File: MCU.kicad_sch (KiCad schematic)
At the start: 1 part, among them U20 STM32H562RGTx

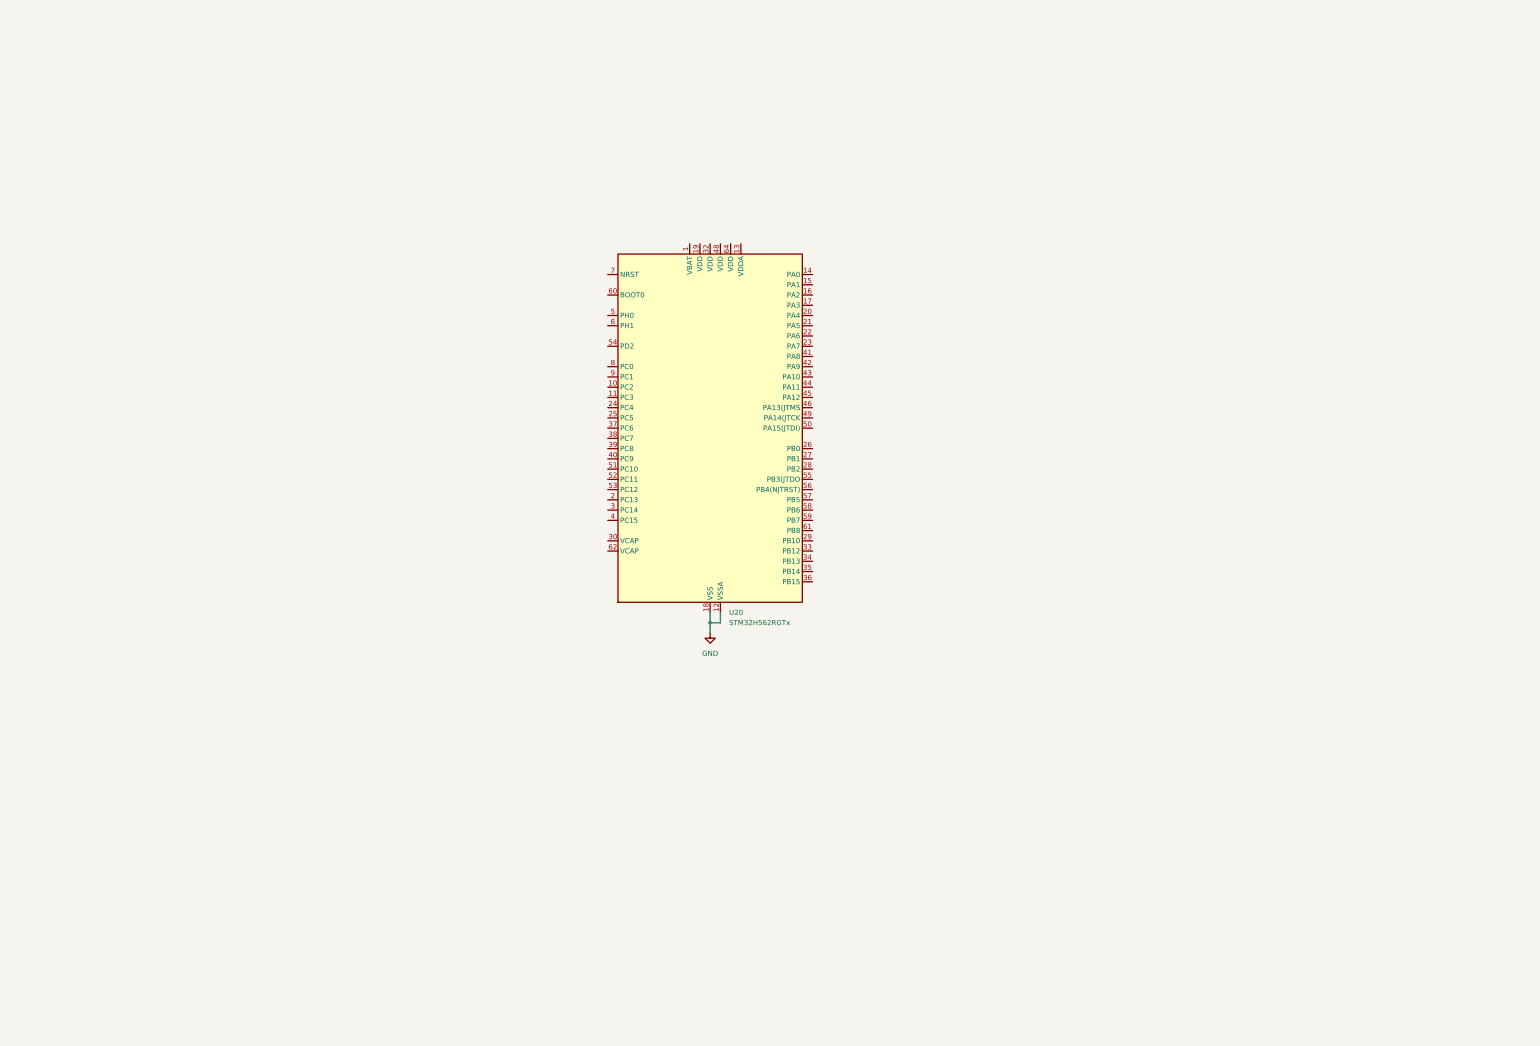
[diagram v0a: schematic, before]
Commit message: almost done with the microcontroller, just need to connect t the AFE and ADC pins
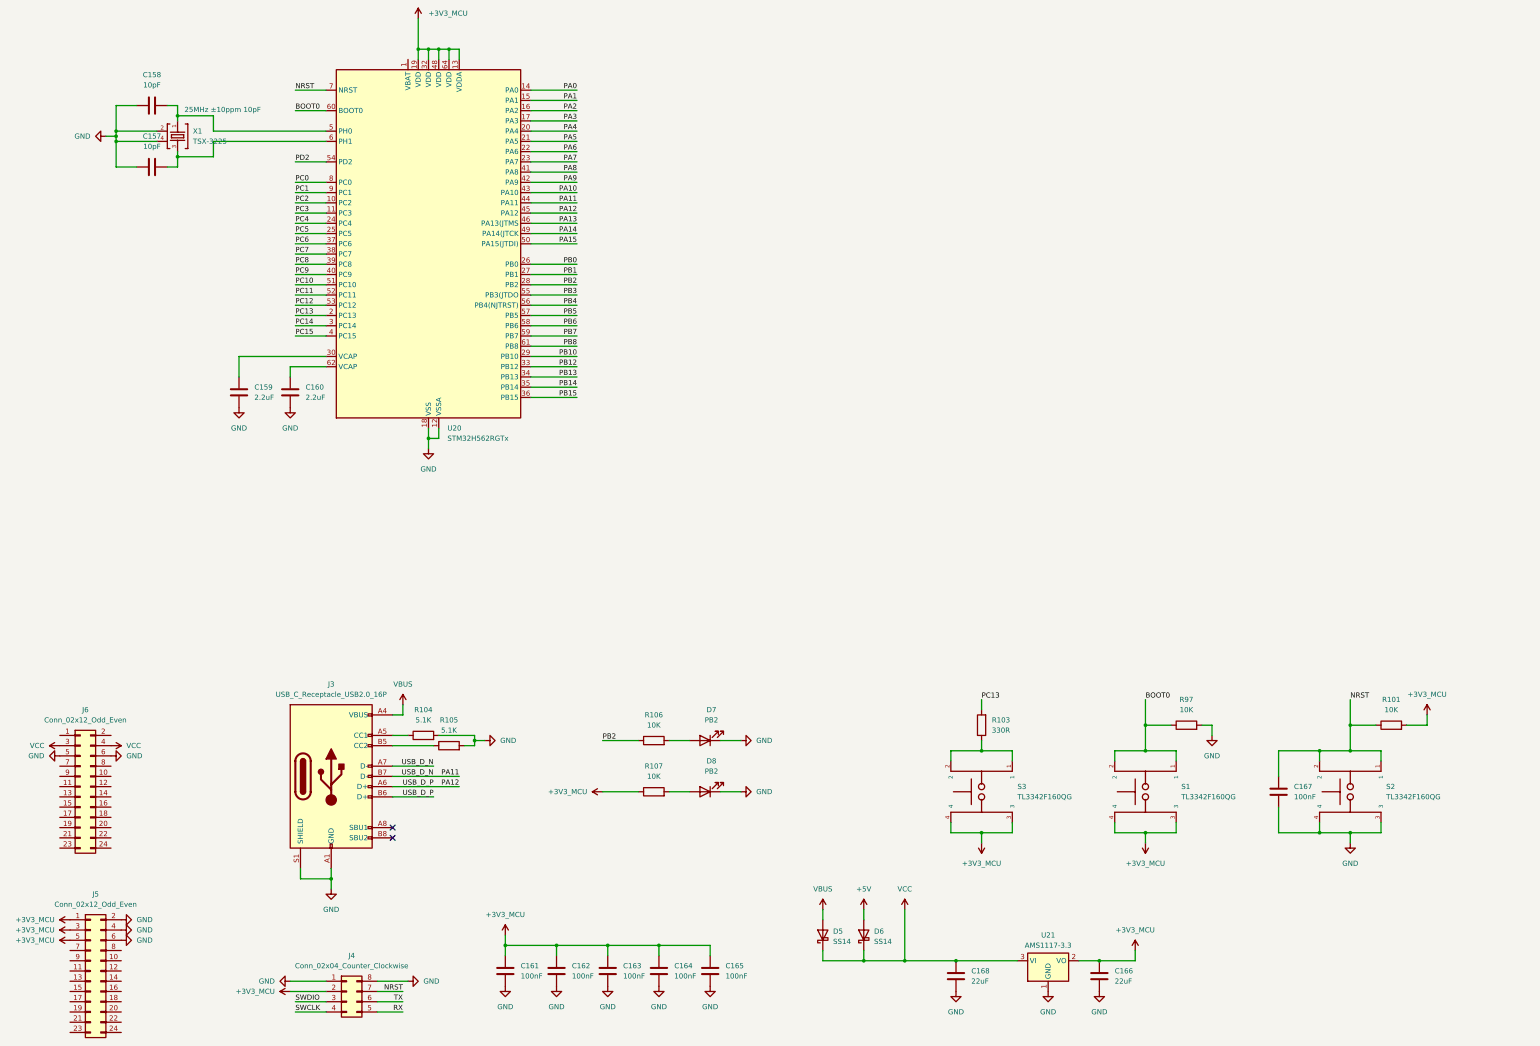
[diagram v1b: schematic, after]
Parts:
- added C157, C158: 10pF, Capacitor_SMD:C_0603_1608Metric_Pad1.08x0.95mm_HandSolder, symbol Device:C
- added C159, C160: 2.2uF, Capacitor_SMD:C_0603_1608Metric_Pad1.08x0.95mm_HandSolder, symbol Device:C
- added C161, C162, C163, C164, C165, C167: 100nF, Capacitor_SMD:C_0603_1608Metric_Pad1.08x0.95mm_HandSolder, symbol Device:C
- added C166, C168: 22uF, Capacitor_SMD:C_0603_1608Metric_Pad1.08x0.95mm_HandSolder, symbol Device:C
- added D5, D6: SS14, Diode_SMD:D_SMA, symbol Diode:SS14
- added D7, D8: PB2, LED_SMD:LED_0603_1608Metric_Pad1.05x0.95mm_HandSolder, symbol Device:LED
- added J3: USB_C_Receptacle_USB2.0_16P, Connector_USB:USB_C_Receptacle_HCTL_HC-TYPE-C-16P-01A, symbol Connector:USB_C_Receptacle_USB2.0_16P
- added J4: Conn_02x04_Counter_Clockwise, Connector_PinHeader_2.54mm:PinHeader_2x04_P2.54mm_Horizontal, symbol Connector_Generic:Conn_02x04_Counter_Clockwise
- added J5, J6: Conn_02x12_Odd_Even, symbol Connector_Generic:Conn_02x12_Odd_Even
- added R101, R106, R107, R97: 10K, Resistor_SMD:R_0603_1608Metric_Pad0.98x0.95mm_HandSolder, symbol Device:R
- added R103: 330R, Resistor_SMD:R_0603_1608Metric_Pad0.98x0.95mm_HandSolder, symbol Device:R
- added R104, R105: 5.1K, Resistor_SMD:R_0603_1608Metric_Pad0.98x0.95mm_HandSolder, symbol Device:R
- added S1, S2, S3: TL3342F160QG, TL3342F160QG:SW_TL3342F160QG, symbol TL3342F160QG:TL3342F160QG
- added U21: AMS1117-3.3, Package_TO_SOT_SMD:SOT-223-3_TabPin2, symbol Regulator_Linear:AMS1117-3.3
- added X1: TSX-3225, TSX-3225:TSX-3225, symbol TSX-3225:TSX-3225
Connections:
- net GND: now also C157.1, C158.2, C159.1, C160.1, C161.2, C162.2, C163.2, C164.2, C165.2, C166.2, C167.2, C168.2, D7.1 (K), D8.1 (K), J3.A1 (GND), J3.A12 (GND), J3.B1 (GND), J3.B12 (GND), J3.S1 (SHIELD), J4.1 (Pin_1), J4.8 (Pin_8), J5.2 (Pin_2), J5.4 (Pin_4), J5.6 (Pin_6), J6.5 (Pin_5), J6.6 (Pin_6), R104.2, R105.2, R97.2, S2.3, S2.4, U21.1 (GND), X1.2, X1.4
- net PC2: now reaches U20.10 (PC2)
- net PC3: now reaches U20.11 (PC3)
- net +3V3_MCU: now reaches U20.13 (VDDA)
- net +3V3_MCU: now also U20.19 (VDD), U20.32 (VDD), U20.48 (VDD), U20.64 (VDD), C161.1, C162.1, C163.1, C164.1, C165.1, C166.1, J4.2 (Pin_2), J5.1 (Pin_1), J5.3 (Pin_3), J5.5 (Pin_5), R101.2, R107.1, S1.3, S1.4, S3.3, S3.4, U21.2 (VO)
- net PA0: now reaches U20.14 (PA0)
- net PA1: now reaches U20.15 (PA1)
- net PA2: now reaches U20.16 (PA2)
- net PA3: now reaches U20.17 (PA3)
- net PC13: now reaches U20.2 (PC13)
- net PC13: now also R103.2
- net PA4: now reaches U20.20 (PA4)
- net PA5: now reaches U20.21 (PA5)
- net PA6: now reaches U20.22 (PA6)
- net PA7: now reaches U20.23 (PA7)
- net PC4: now reaches U20.24 (PC4)
- net PC5: now reaches U20.25 (PC5)
- net PB0: now reaches U20.26 (PB0)
- net PB1: now reaches U20.27 (PB1)
- net PB2: now reaches U20.28 (PB2)
- net PB2: now also R106.1
- net PB10: now reaches U20.29 (PB10)
- net PC14: now reaches U20.3 (PC14)
- net at U20.30 (VCAP): now also C159.2
- net PB12: now reaches U20.33 (PB12)
- net PB13: now reaches U20.34 (PB13)
- net PB14: now reaches U20.35 (PB14)
- net PB15: now reaches U20.36 (PB15)
- net PC6: now reaches U20.37 (PC6)
- net PC7: now reaches U20.38 (PC7)
- net PC8: now reaches U20.39 (PC8)
- net PC15: now reaches U20.4 (PC15)
- net PC9: now reaches U20.40 (PC9)
- net PA8: now reaches U20.41 (PA8)
- net PA9: now reaches U20.42 (PA9)
- net PA10: now reaches U20.43 (PA10)
- net PA11: now reaches U20.44 (PA11)
- net PA11: now also J3.A7 (D-), J3.B7 (D-)
- net PA12: now reaches U20.45 (PA12)
- net PA12: now also J3.A6 (D+), J3.B6 (D+)
- net PA13: now reaches U20.46 (PA13(JTMS)
- net PA14: now reaches U20.49 (PA14(JTCK)
- net at U20.5 (PH0): now also C158.1, X1.1
- net PA15: now reaches U20.50 (PA15(JTDI))
- net PC10: now reaches U20.51 (PC10)
- net PC11: now reaches U20.52 (PC11)
- net PC12: now reaches U20.53 (PC12)
- net PD2: now reaches U20.54 (PD2)
- net PB3: now reaches U20.55 (PB3(JTDO)
- net PB4: now reaches U20.56 (PB4(NJTRST))
- net PB5: now reaches U20.57 (PB5)
- net PB6: now reaches U20.58 (PB6)
- net PB7: now reaches U20.59 (PB7)
- net at U20.6 (PH1): now also C157.2, X1.3
- net BOOT0: now reaches U20.60 (BOOT0)
- net BOOT0: now also R97.1, S1.1, S1.2
- net PB8: now reaches U20.61 (PB8)
- net at U20.62 (VCAP): now also C160.2
- net NRST: now reaches U20.7 (NRST)
- net NRST: now also C167.1, J4.7 (Pin_7), R101.1, S2.1, S2.2
- net PC0: now reaches U20.8 (PC0)
- net PC1: now reaches U20.9 (PC1)
- new net: D8.2 (A), R107.2
- new net: J3.A5 (CC1), R104.1
- new net: R103.1, S3.1, S3.2
- new net: J3.B5 (CC2), R105.1
- new net: D7.2 (A), R106.2
- new net +5V: D6.2 (A)
- new net RX: J4.5 (Pin_5)
- new net SWCLK: J4.4 (Pin_4)
- new net SWDIO: J4.3 (Pin_3)
- new net TX: J4.6 (Pin_6)
- new net VBUS: D5.2 (A), J3.A4 (VBUS), J3.A9 (VBUS), J3.B4 (VBUS), J3.B9 (VBUS)
- new net VCC: C168.1, D5.1 (K), D6.1 (K), J6.3 (Pin_3), J6.4 (Pin_4), U21.3 (VI)
- no-connect marks 0 -> 2
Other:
- moved on the sheet: U20

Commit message: schematic complete. no ERC errors
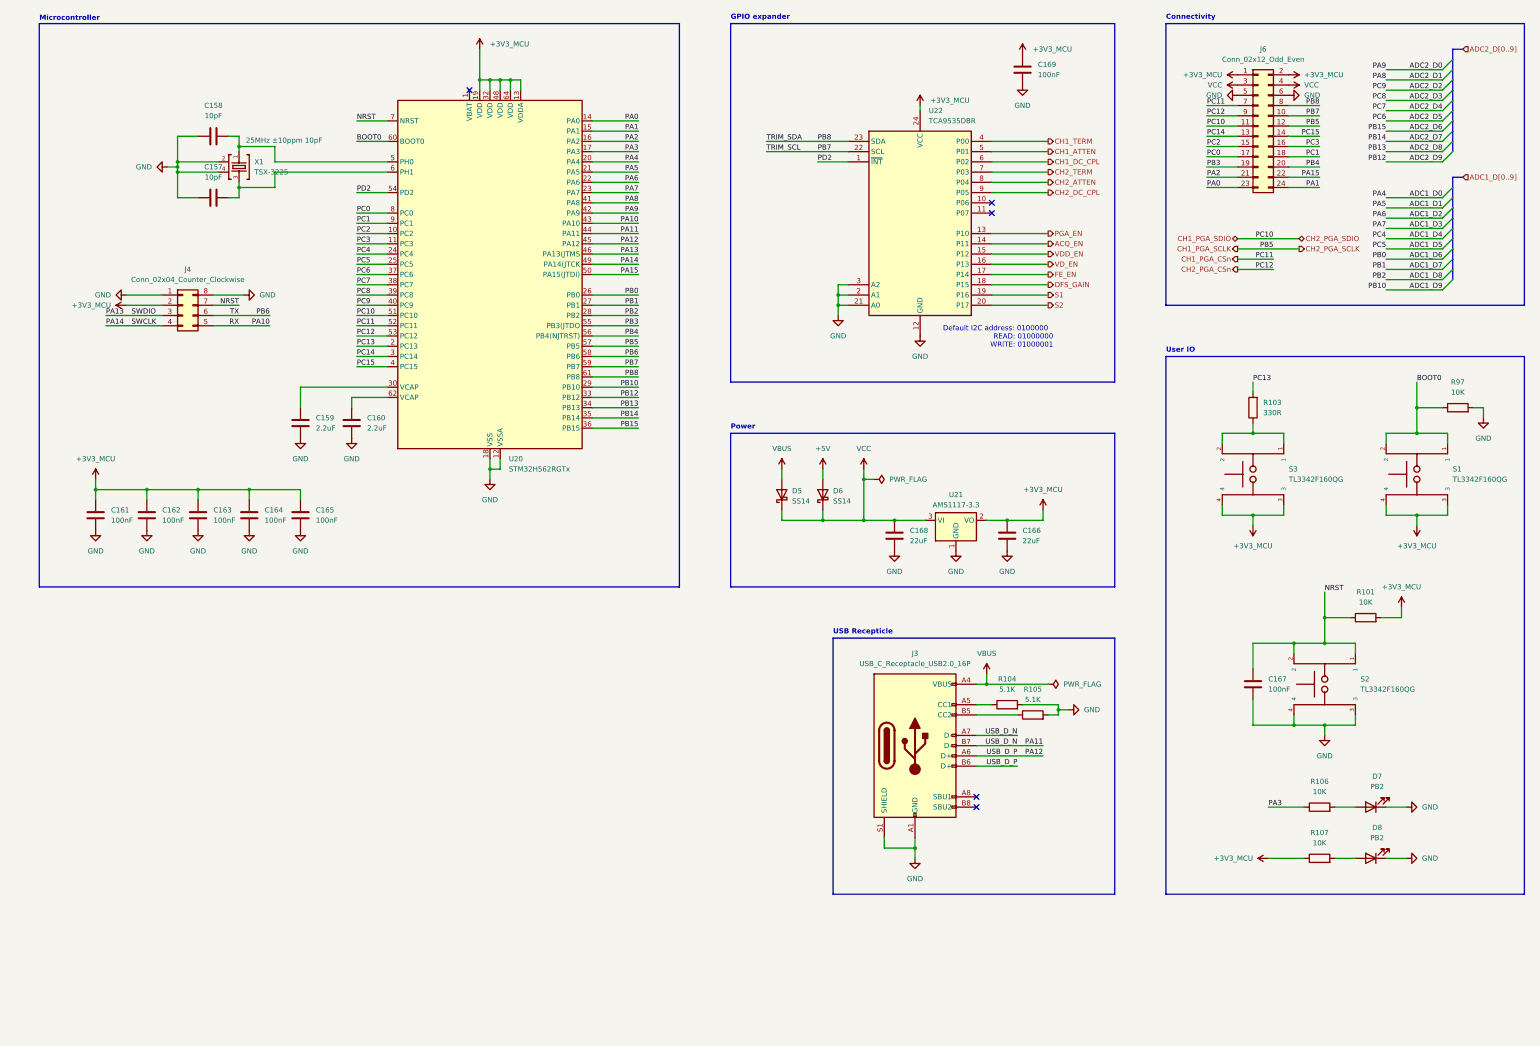
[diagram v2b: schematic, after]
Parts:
- removed J5: Conn_02x12_Odd_Even, symbol Connector_Generic:Conn_02x12_Odd_Even
- added C169: 100nF, Capacitor_SMD:C_0603_1608Metric_Pad1.08x0.95mm_HandSolder, symbol Device:C
- added U22: TCA9535DBR, Package_SO:SSOP-24_5.3x8.2mm_P0.65mm, symbol Interface_Expansion:TCA9535DBR
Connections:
- net PB5 is gone; now on net CH1_PGA_SCLK: U20.57 (PB5)
- net PC10 is gone; now on net CH1_PGA_SDIO: U20.51 (PC10)
- net PC11 is gone; now on net CH1_PGA_CSn: U20.52 (PC11)
- net PC12 is gone; now on net CH2_PGA_CSn: U20.53 (PC12)
- net RX is gone; now on net PA10: J4.5 (Pin_5)
- net SWCLK is gone; now on net PA14: J4.4 (Pin_4)
- net SWDIO is gone; now on net PA13: J4.3 (Pin_3)
- net TX is gone; now on net PB6: J4.6 (Pin_6)
- net +3V3_MCU: now also J6.1 (Pin_1), J6.2 (Pin_2), C169.1, U22.24 (VCC)
- net GND: now also C169.2, U22.12 (GND), U22.2 (A1), U22.21 (A0), U22.3 (A2)
- net PA0: now also J6.23 (Pin_23)
- net PA1: now also J6.24 (Pin_24)
- net PA15: now also J6.22 (Pin_22)
- net PA2: now also J6.21 (Pin_21)
- net PA3: now also R106.1
- net PB3: now also J6.19 (Pin_19)
- net PB4: now also J6.20 (Pin_20)
- net PB7: now also J6.10 (Pin_10), U22.22 (SCL)
- net PB8: now also J6.8 (Pin_8), U22.23 (SDA)
- net PC0: now also J6.17 (Pin_17)
- net PC1: now also J6.18 (Pin_18)
- net PC14: now also J6.13 (Pin_13)
- net PC15: now also J6.14 (Pin_14)
- net PC2: now also J6.15 (Pin_15)
- net PC3: now also J6.16 (Pin_16)
- net PD2: now also U22.1 (~{INT})
- net CH1_PGA_SDIO: now reaches J6.11 (Pin_11)
- net CH1_PGA_SCLK: now reaches J6.12 (Pin_12)
- net CH1_PGA_CSn: now reaches J6.7 (Pin_7)
- net CH2_PGA_CSn: now reaches J6.9 (Pin_9)
- net PA4 renamed ADC1_D0
- net PA5 renamed ADC1_D1
- net PA6 renamed ADC1_D2
- net PA7 renamed ADC1_D3
- net PA8 renamed ADC2_D1
- net PA9 renamed ADC2_D0
- net PB0 renamed ADC1_D6
- net PB1 renamed ADC1_D7
- net PB10 renamed ADC1_D9
- net PB12 renamed ADC2_D9
- net PB13 renamed ADC2_D8
- net PB14 renamed ADC2_D7
- net PB15 renamed ADC2_D6
- net PB2 renamed ADC1_D8
- net ADC1_D8: no longer R106.1
- net PC4 renamed ADC1_D4
- net PC5 renamed ADC1_D5
- net PC6 renamed ADC2_D5
- net PC7 renamed ADC2_D4
- net PC8 renamed ADC2_D3
- net PC9 renamed ADC2_D2
- new net ACQ_EN: U22.14 (P11)
- new net CH1_ATTEN: U22.5 (P01)
- new net CH1_DC_CPL: U22.6 (P02)
- new net CH1_TERM: U22.4 (P00)
- new net CH2_ATTEN: U22.8 (P04)
- new net CH2_DC_CPL: U22.9 (P05)
- new net CH2_TERM: U22.7 (P03)
- new net DFS_GAIN: U22.18 (P15)
- new net FE_EN: U22.17 (P14)
- new net PGA_EN: U22.13 (P10)
- new net S1: U22.19 (P16)
- new net S2: U22.20 (P17)
- new net VDD_EN: U22.15 (P12)
- new net VD_EN: U22.16 (P13)
- no-connect marks 2 -> 5
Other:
- note added: "Connectivity"
- note added: "Default I2C address: 0100000"
- note added: "GPIO expander"
- note added: "Microcontroller"
- note added: "Power"
- note added: "READ: 01000000"
- note added: "USB Recepticle"
- note added: "User IO"
- note added: "WRITE: 01000001"
- moved on the sheet: C157, C158, C159, C160, C161, C162, C163, C164, C165, C166, C167, C168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
